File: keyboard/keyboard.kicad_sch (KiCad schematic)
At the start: 133 parts, among them J1 USB_C_Receptacle_USB2.0, J2 Programmer 1 time, J3 Addon interface, J4 Digital NOB, Q1 PMOS, SW1 SW_DIP_x01, U1 ATmega32U4-M, Y1 7F16000E09UCG

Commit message: battery connectors with diodes. (Should be replaced to FETs before production)
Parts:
- removed D4: 5V Zener, Diode_SMD:D_SOD-523, symbol Device:D_Zener
- removed Q1: PMOS, Package_TO_SOT_SMD:TO-252-2, symbol Simulation_SPICE:PMOS
- removed R10: R100K, Resistor_SMD:R_0402_1005Metric, symbol Device:R
- added D4: D, Diode_SMD:D_0402_1005Metric, symbol Device:D
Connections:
- net VCC: now also D4.1 (K); no longer D5.2 (A)
- net POWER_IN renamed VIN
- net VIN: now also D5.2 (A), D4.2 (A)
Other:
- moved on the sheet: J1, R1, R2, R6, R7, R8

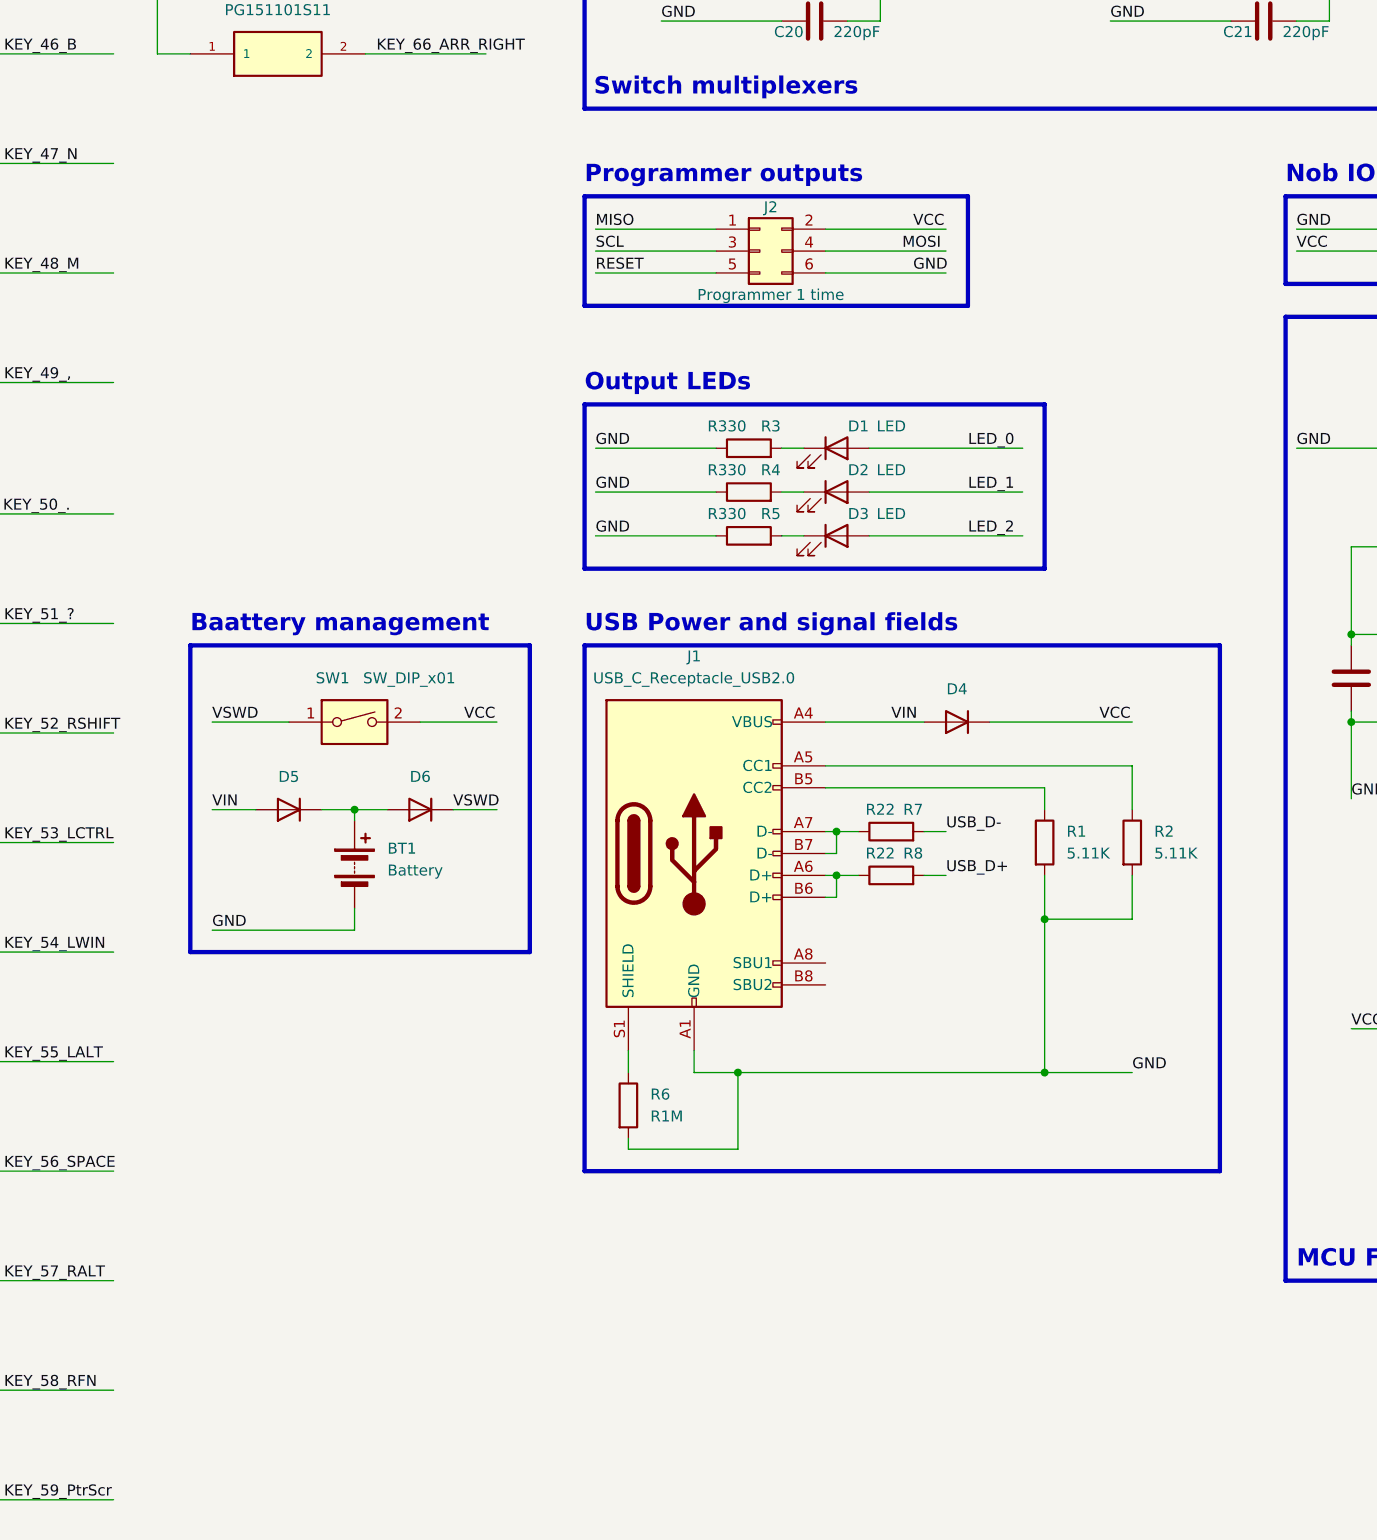
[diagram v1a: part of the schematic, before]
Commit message: Remove unnecessary files and add pullups for arrow keys.
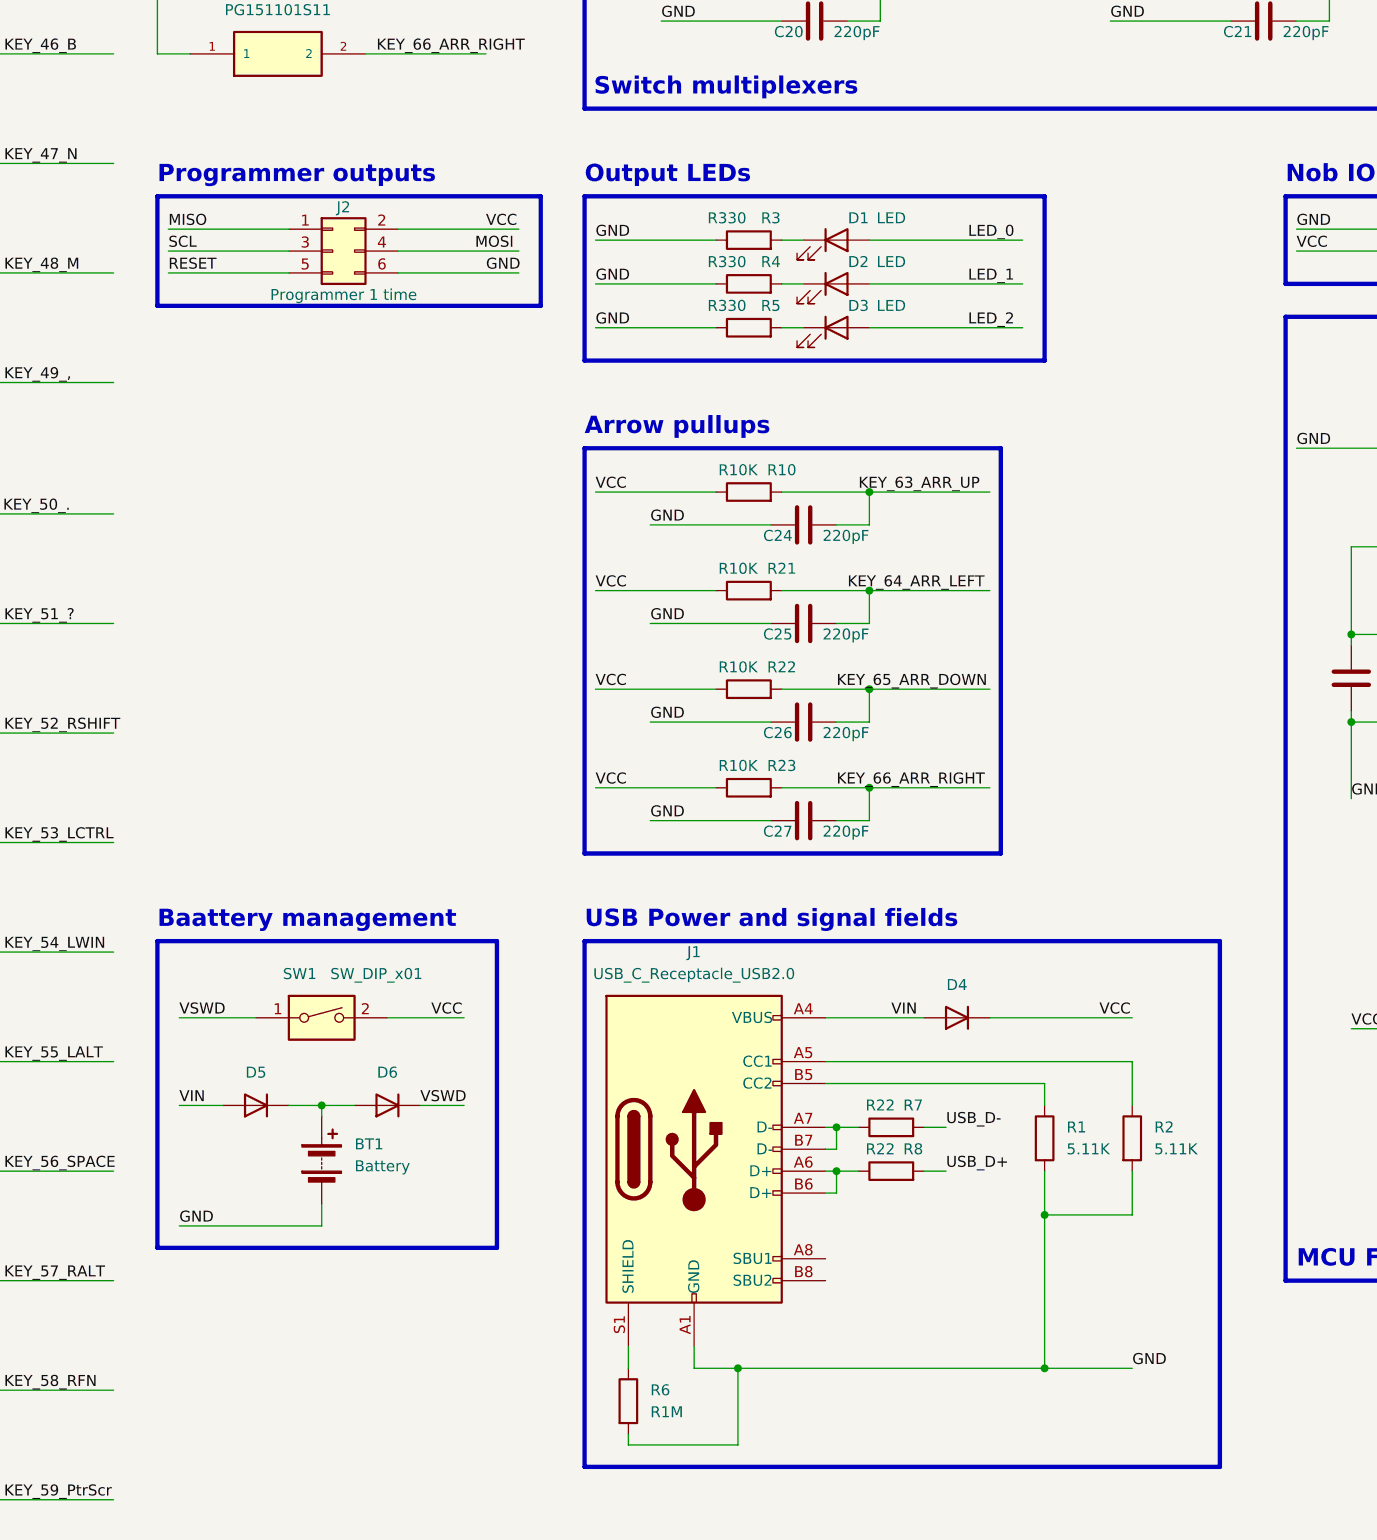
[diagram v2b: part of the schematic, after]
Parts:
- added C24, C25, C26, C27: 220pF, Capacitor_SMD:C_0402_1005Metric, symbol Device:C
- added R10, R21, R22, R23: R10K, Resistor_SMD:R_0402_1005Metric, symbol Device:R
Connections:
- net GND: now also C24.1, C25.1, C26.1, C27.1
- net KEY_63_ARR_UP: now also C24.2, R10.2
- net KEY_64_ARR_LEFT: now also C25.2, R21.2
- net KEY_65_ARR_DOWN: now also C26.2, R22.2
- net KEY_66_ARR_RIGHT: now also C27.2, R23.2
- net VCC: now also R10.1, R21.1, R22.1, R23.1
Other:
- note added: "Arrow pullups"
- moved on the sheet: BT1, D1, D2, D3, D4, D5, D6, J1, J2, R1, R2, R3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

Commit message: Battery planning
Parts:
- removed BT1: Battery, Connector_PinHeader_2.54mm:PinHeader_1x02_P2.54mm_Vertical, symbol Device:Battery
- removed D5, D6: D, Diode_SMD:D_0402_1005Metric, symbol Device:D
- removed SW1: SW_DIP_x01, Connector_PinHeader_2.54mm:PinHeader_1x02_P2.54mm_Vertical, symbol Switch:SW_DIP_x01
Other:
- added sheet Bettery management and USB hub (battery_usb.kicad_sch)
- note removed: "Baattery management"
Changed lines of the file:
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@@
   (junction (at 148.59 58.42) (diameter 0) (color 0 0 0 0)
   )
-  (junction (at 167.64 231.14) (diameter 0) (color 0 0 0 0)
-  )
   (junction (at 317.5 142.24) (diameter 0) (color 0 0 0 0)
   )
@@
     (stroke (width 0) (type default))
   )
-  (wire (pts (xy 175.26 220.98) (xy 184.15 220.98))
-    (stroke (width 0) (type default))
-  )
   (wire (pts (xy 172.72 33.02) (xy 186.69 33.02))
     (stroke (width 0) (type default))
@@
     (stroke (width 0) (type default))
   )
-  (wire (pts (xy 151.13 220.98) (xy 160.02 220.98))
-    (stroke (width 0) (type default))
-  )
   (wire (pts (xy 364.49 44.45) (xy 364.49 45.72))
     (stroke (width 0) (type default))
@@
     (stroke (width 0) (type default))
   )
-  (wire (pts (xy 179.07 231.14) (xy 184.15 231.14))
-    (stroke (width 0) (type default))
-  )
   (wire (pts (xy 105.41 147.32) (xy 105.41 162.56))
     (stroke (width 0) (type default))
@@
     (stroke (width 0) (type default))
   )
-  (wire (pts (xy 171.45 231.14) (xy 167.64 231.14))
-    (stroke (width 0) (type default))
-  )
   (wire (pts (xy 19.05 109.22) (xy 22.86 109.22))
     (stroke (width 0) (type default))
@@
     (stroke (width 0) (type default))
   )
-  (wire (pts (xy 167.64 232.41) (xy 167.64 231.14))
-    (stroke (width 0) (type default))
-  )
   (wire (pts (xy 86.36 147.32) (xy 100.33 147.32))
     (stroke (width 0) (type default))
@@
     (stroke (width 0) (type default))
   )
-  (wire (pts (xy 163.83 231.14) (xy 167.64 231.14))
-    (stroke (width 0) (type default))
-  )
   (wire (pts (xy 19.05 17.78) (xy 19.05 33.02))
     (stroke (width 0) (type default))
@@
     (stroke (width 0) (type default))
   )
-  (wire (pts (xy 151.13 245.11) (xy 167.64 245.11))
-    (stroke (width 0) (type default))
-  )
   (wire (pts (xy 312.42 45.72) (xy 316.23 45.72))
     (stroke (width 0) (type default))
@@
     (stroke (width 0) (type default))
   )
-  (wire (pts (xy 151.13 231.14) (xy 156.21 231.14))
-    (stroke (width 0) (type default))
-  )
   (wire (pts (xy 226.06 228.6) (xy 251.46 228.6))
     (stroke (width 0) (type default))
@@
     (stroke (width 0) (type default))
   )
-  (wire (pts (xy 167.64 242.57) (xy 167.64 245.11))
-    (stroke (width 0) (type default))
-  )
   (wire (pts (xy 336.55 72.39) (xy 350.52 72.39))
     (stroke (width 0) (type default))
@@
     (fill (type none))
   )
-  (rectangle (start 148.59 212.09) (end 187.96 247.65)
-    (stroke (width 0.5) (type default) (color 59 93 255 1))
-    (fill (type none))
-  )
-  (text "Baattery management" (at 148.59 210.82 0)
-    (effects (font (size 2 2) (thickness 0.254) bold (color 59 93 255 1)) (justify left bottom))
-  )
   (text "MCU Fields" (at 280.67 250.19 0)
     (effects (font (size 2 2) (thickness 0.254) bold (color 59 93 255 1)) (justify left bottom))
@@
     (effects (font (size 1.27 1.27)) (justify left bottom))
   )
-  (label "VSWD" (at 151.13 220.98 0) (fields_autoplaced)
-    (effects (font (size 1.27 1.27)) (justify left bottom))
-  )
   (label "VCC" (at 330.2 132.08 0) (fields_autoplaced)
     (effects (font (size 1.27 1.27)) (justify left bottom))
@@
     (effects (font (size 1.27 1.27)) (justify left bottom))
   )
-  (label "VIN" (at 151.13 231.14 0) (fields_autoplaced)
-    (effects (font (size 1.27 1.27)) (justify left bottom))
-  )
   (label "KEY_54_LWIN" (at 130.81 213.36 0) (fields_autoplaced)
     (effects (font (size 1.27 1.27)) (justify left bottom))
@@
     (effects (font (size 1.27 1.27)) (justify left bottom))
   )
-  (label "VCC" (at 180.34 220.98 0) (fields_autoplaced)
-    (effects (font (size 1.27 1.27)) (justify left bottom))
-  )
   (label "VCC" (at 186.69 129.54 0) (fields_autoplaced)
     (effects (font (size 1.27 1.27)) (justify left bottom))
@@
     (effects (font (size 1.27 1.27)) (justify left bottom))
   )
-  (label "VSWD" (at 179.07 231.14 0) (fields_autoplaced)
-    (effects (font (size 1.27 1.27)) (justify left bottom))
-  )
   (label "GND" (at 280.67 129.54 0) (fields_autoplaced)
     (effects (font (size 1.27 1.27)) (justify left bottom))
@@
     (effects (font (size 1.27 1.27)) (justify left bottom))
   )
-  (label "GND" (at 151.13 245.11 0) (fields_autoplaced)
-    (effects (font (size 1.27 1.27)) (justify left bottom))
-  )
   (label "VCC" (at 252.73 36.83 0) (fields_autoplaced)
     (effects (font (size 1.27 1.27)) (justify left bottom))
@@
     )
   )
-  (symbol (lib_id "Switch:SW_DIP_x01") (at 167.64 220.98 0) (unit 1)
-    (in_bom yes) (on_board yes) (dnp no)
-    (property "Reference" "SW1" (at 165.1 215.9 0)
-      (effects (font (size 1.27 1.27)))
-    )
-    (property "Value" "SW_DIP_x01" (at 173.99 215.9 0)
-      (effects (font (size 1.27 1.27)))
-    )
-    (property "Footprint" "Connector_PinHeader_2.54mm:PinHeader_1x02_P2.54mm_Vertical" (at 167.64 220.98 0)
-      (effects (font (size 1.27 1.27)) hide)
-    )
-    (property "Datasheet" "~" (at 167.64 220.98 0)
-      (effects (font (size 1.27 1.27)) hide)
-    )
-    (pin "1")
-    (pin "2")
-    (instances
-      (project "keyboard"
-        (path "/ba343d94-601d-44c5-b848-a7d9121c7be9"
-          (reference "SW1") (unit 1)
-        )
-      )
-    )
-  )
   (symbol (lib_id "PG151101S11:PG151101S11") (at 33.02 58.42 0) (unit 1)
     (in_bom yes) (on_board yes) (dnp no) (fields_autoplaced)
@@
     )
   )
-  (symbol (lib_id "Device:D") (at 175.26 231.14 180) (unit 1)
-    (in_bom yes) (on_board yes) (dnp no)
-    (property "Reference" "D6" (at 175.26 227.33 0)
-      (effects (font (size 1.27 1.27)))
-    )
-    (property "Value" "D" (at 173.99 227.33 0)
-      (effects (font (size 1.27 1.27)) hide)
-    )
-    (property "Footprint" "Diode_SMD:D_0402_1005Metric" (at 175.26 231.14 0)
-      (effects (font (size 1.27 1.27)) hide)
-    )
-    (property "Datasheet" "~" (at 175.26 231.14 0)
-      (effects (font (size 1.27 1.27)) hide)
-    )
-    (property "Sim.Device" "D" (at 175.26 231.14 0)
-      (effects (font (size 1.27 1.27)) hide)
-    )
-    (property "Sim.Pins" "1=K 2=A" (at 175.26 231.14 0)
-      (effects (font (size 1.27 1.27)) hide)
-    )
-    (pin "1")
-    (pin "2")
-    (instances
-      (project "keyboard"
-        (path "/ba343d94-601d-44c5-b848-a7d9121c7be9"
-          (reference "D6") (unit 1)
-        )
-      )
-    )
-  )
   (symbol (lib_id "Device:R") (at 322.58 101.6 90) (unit 1)
     (in_bom yes) (on_board yes) (dnp no)
@@
     )
   )
-  (symbol (lib_id "Device:D") (at 160.02 231.14 180) (unit 1)
-    (in_bom yes) (on_board yes) (dnp no)
-    (property "Reference" "D5" (at 160.02 227.33 0)
-      (effects (font (size 1.27 1.27)))
-    )
-    (property "Value" "D" (at 158.75 227.33 0)
-      (effects (font (size 1.27 1.27)) hide)
-    )
-    (property "Footprint" "Diode_SMD:D_0402_1005Metric" (at 160.02 231.14 0)
-      (effects (font (size 1.27 1.27)) hide)
-    )
-    (property "Datasheet" "~" (at 160.02 231.14 0)
-      (effects (font (size 1.27 1.27)) hide)
-    )
-    (property "Sim.Device" "D" (at 160.02 231.14 0)
-      (effects (font (size 1.27 1.27)) hide)
-    )
-    (property "Sim.Pins" "1=K 2=A" (at 160.02 231.14 0)
-      (effects (font (size 1.27 1.27)) hide)
-    )
-    (pin "1")
-    (pin "2")
-    (instances
-      (project "keyboard"
-        (path "/ba343d94-601d-44c5-b848-a7d9121c7be9"
-          (reference "D5") (unit 1)
-        )
-      )
-    )
-  )
   (symbol (lib_id "Device:C") (at 276.86 105.41 90) (unit 1)
     (in_bom yes) (on_board yes) (dnp no)
@@
     )
   )
-  (symbol (lib_id "Device:Battery") (at 167.64 237.49 0) (unit 1)
-    (in_bom yes) (on_board yes) (dnp no) (fields_autoplaced)
-    (property "Reference" "BT1" (at 171.45 235.6485 0)
-      (effects (font (size 1.27 1.27)) (justify left))
-    )
-    (property "Value" "Battery" (at 171.45 238.1885 0)
-      (effects (font (size 1.27 1.27)) (justify left))
-    )
-    (property "Footprint" "Connector_PinHeader_2.54mm:PinHeader_1x02_P2.54mm_Vertical" (at 167.64 235.966 90)
-      (effects (font (size 1.27 1.27)) hide)
-    )
-    (property "Datasheet" "~" (at 167.64 235.966 90)
-      (effects (font (size 1.27 1.27)) hide)
-    )
-    (pin "1")
-    (pin "2")
-    (instances
-      (project "keyboard"
-        (path "/ba343d94-601d-44c5-b848-a7d9121c7be9"
-          (reference "BT1") (unit 1)
-        )
-      )
-    )
-  )
   (symbol (lib_id "PG151101S11:PG151101S11") (at 119.38 200.66 0) (unit 1)
     (in_bom yes) (on_board yes) (dnp no) (fields_autoplaced)
@@
       )
     )
+  )
+  (sheet (at 151.13 250.19) (size 39.37 22.86) (fields_autoplaced)
+    (stroke (width 0.1524) (type solid))
+    (fill (color 0 0 0 0.0000))
+    (property "Sheetname" "Bettery management and USB hub" (at 151.13 249.4784 0)
+      (effects (font (size 1.27 1.27)) (justify left bottom))
+    )
+    (property "Sheetfile" "battery_usb.kicad_sch" (at 151.13 273.6346 0)
+      (effects (font (size 1.27 1.27)) (justify left top))
+    )
+    (instances
+      (project "keyboard"
+        (path "/ba343d94-601d-44c5-b848-a7d9121c7be9" (page "2"))
+      )
+    )
